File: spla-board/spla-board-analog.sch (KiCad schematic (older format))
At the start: 99 parts, among them J13 J_ANALOG, J14 J_AREF, J8 J_AREF_AMP, U51 ADC1173, U52 ADC1173, U53 ADC1173, U61 LMH6611, U62 LMH6611, U63 LMH6611, U74 LMH6611, U75 LMH6611, U76 TLV73333PDBV

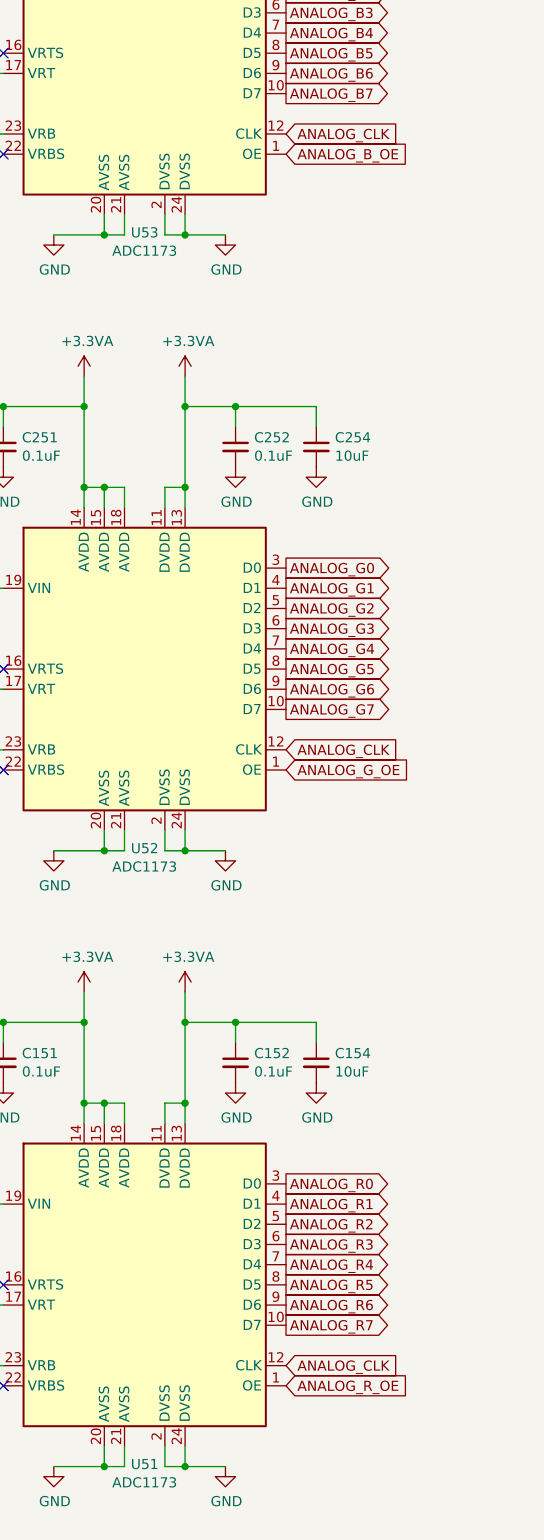
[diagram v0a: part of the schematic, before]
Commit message: schematic/pcb: Consolidate analog output-enable nets, and add a pullup resistor.
Note that this leaves two FPGA pins unused, which I'll need to correct later.
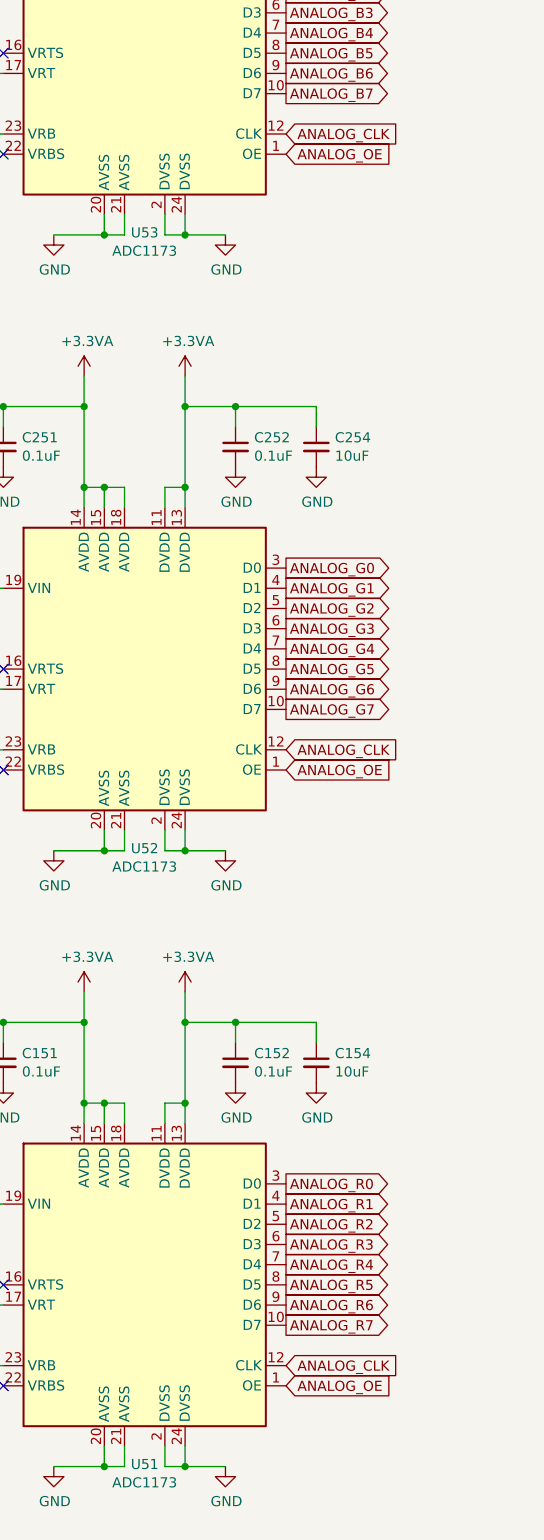
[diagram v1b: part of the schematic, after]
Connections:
- net ANALOG_G_OE is gone; now on net ANALOG_OE: U52.1 (OE)
- net ANALOG_R_OE is gone; now on net ANALOG_OE: U51.1 (OE)
- net ANALOG_B_OE renamed ANALOG_OE
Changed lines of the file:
@@
 RC low-pass filter\nCutoff = 1/(2*pi*R109*C109) = 18.55MHz\nWith Rxxx = 22 and Cxxx = 390pF\nNOSTUFF for now; left in as an option.
 Text GLabel 15000 3050 2    50   Input ~ 0
-ANALOG_B_OE
+ANALOG_OE
 Text GLabel 15000 6100 2    50   Input ~ 0
-ANALOG_G_OE
+ANALOG_OE
 Text GLabel 15000 9150 2    50   Input ~ 0
-ANALOG_R_OE
+ANALOG_OE
 Wire Wire Line
 	9450 7050 9450 7150

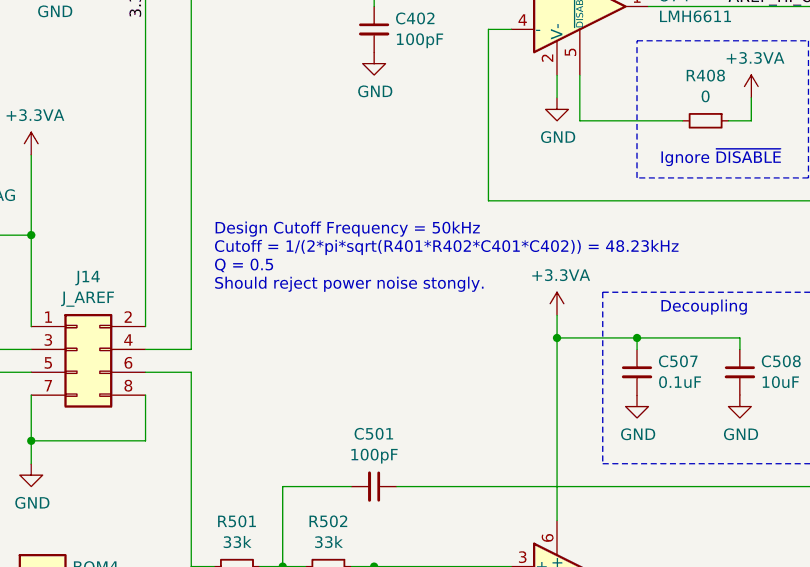
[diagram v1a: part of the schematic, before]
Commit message: schematic: Fix typo.
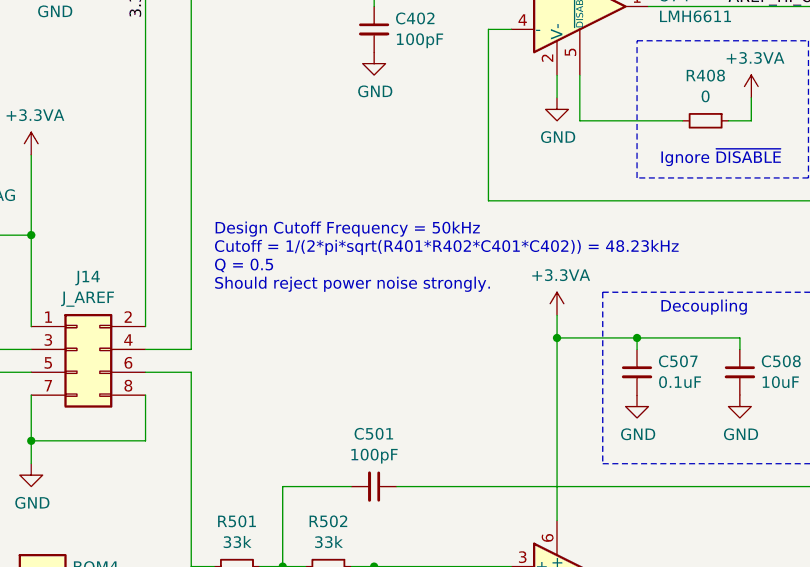
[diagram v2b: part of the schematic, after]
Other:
- note added: "Design Cutoff Frequency = 50kHz\nCutoff = 1/(2*pi*sqrt(R401*R402*C401*C402)) = 48.23kHz\nQ = 0.5\nShould reject power noise strongly."
- note removed: "Design Cutoff Frequency = 50kHz\nCutoff = 1/(2*pi*sqrt(R401*R402*C401*C402)) = 48.23kHz\nQ = 0.5\nShould reject power noise stongly."
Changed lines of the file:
@@
 Ignore ~DISABLE~
 Text Notes 2700 8600 0    50   ~ 0
-Design Cutoff Frequency = 50kHz\nCutoff = 1/(2*pi*sqrt(R401*R402*C401*C402)) = 48.23kHz\nQ = 0.5\nShould reject power noise stongly.
+Design Cutoff Frequency = 50kHz\nCutoff = 1/(2*pi*sqrt(R401*R402*C401*C402)) = 48.23kHz\nQ = 0.5\nShould reject power noise strongly.
 Wire Wire Line
 	4200 6150 4200 6250

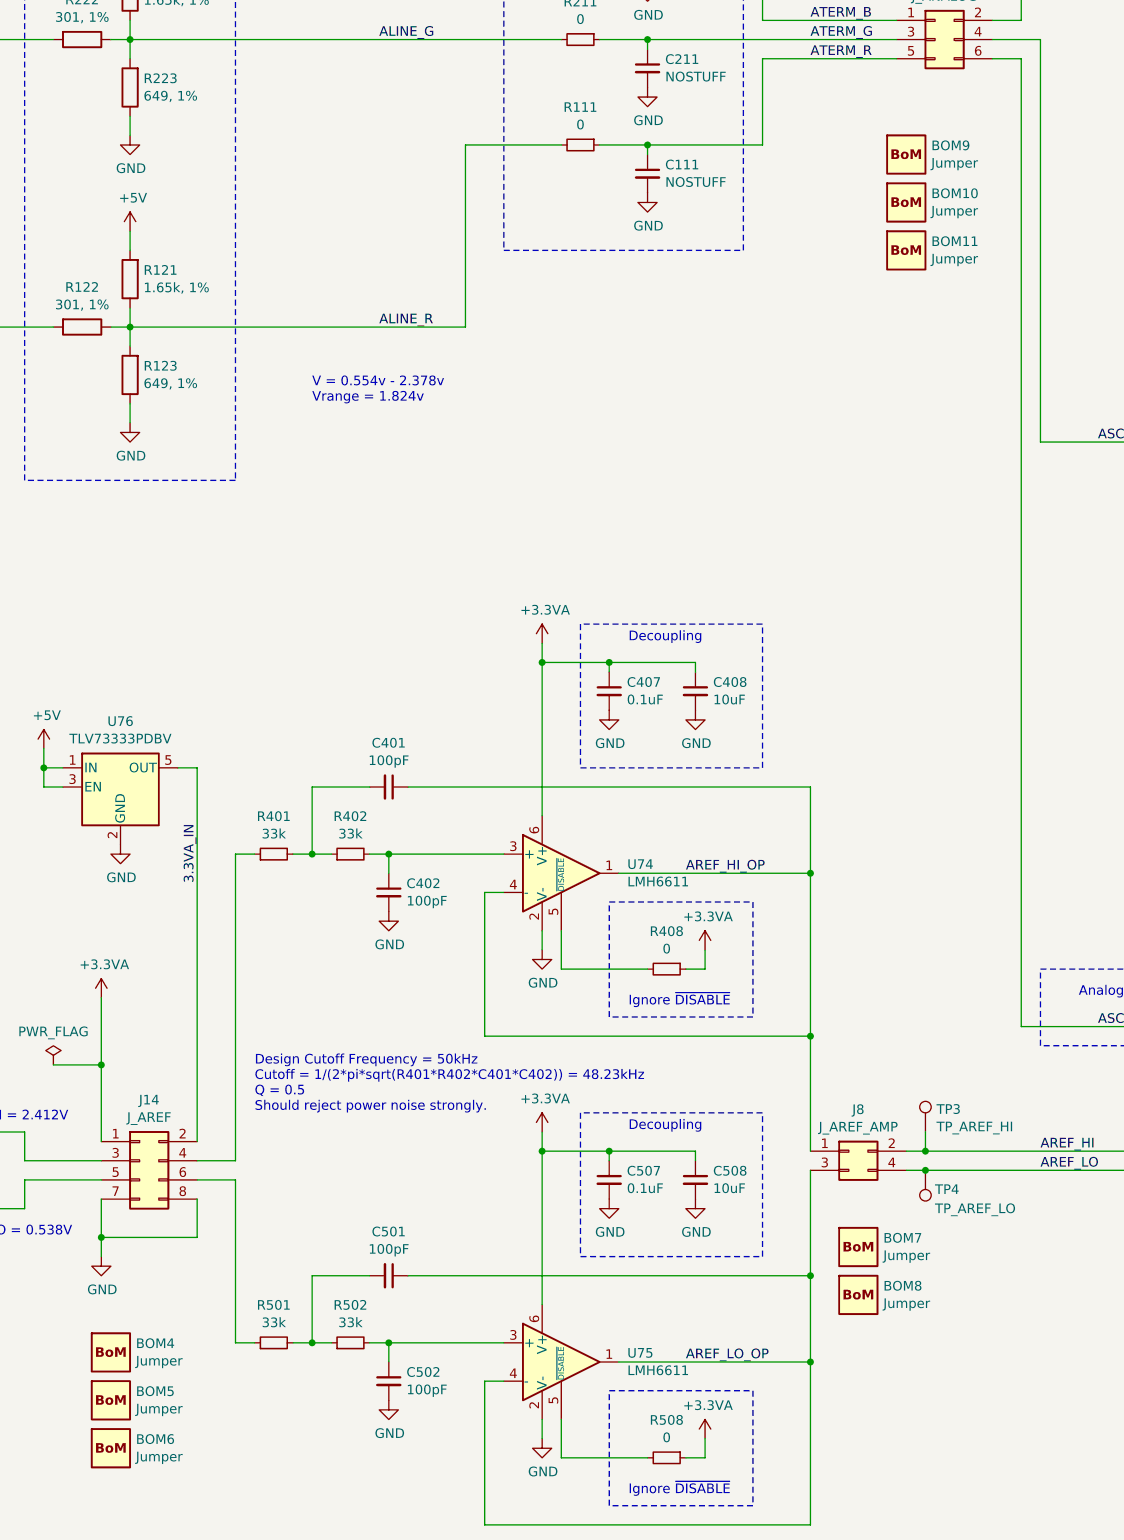
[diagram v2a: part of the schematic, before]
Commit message: schematic/pcb: Remove unnecessary 0-ohm resistors; renumber all parts by value.
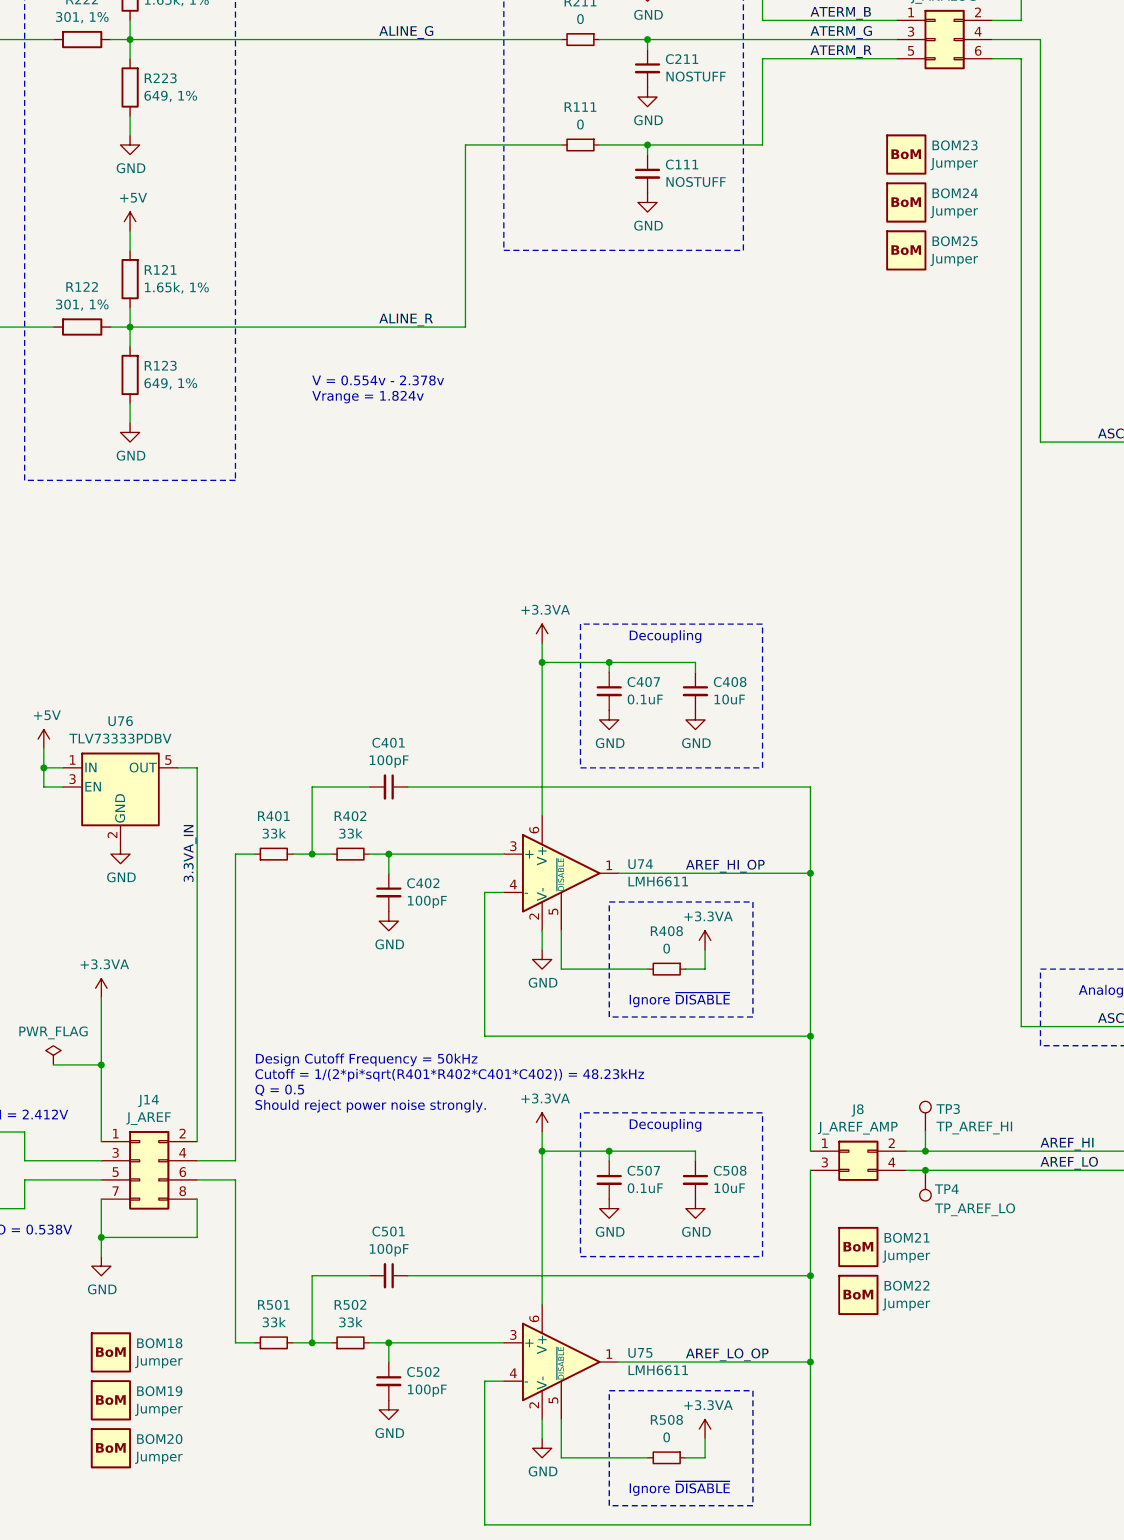
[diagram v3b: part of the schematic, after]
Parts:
- renumbered BOM4 to BOM18, BOM5 to BOM19, BOM6 to BOM20, BOM7 to BOM21, BOM8 to BOM22, BOM9 to BOM23, BOM10 to BOM24, BOM11 to BOM25
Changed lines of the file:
@@
 P 1950 9850
 AR Path="/5E50E589/5EB18261" Ref="BOM?"  Part="1"
-AR Path="/5E520B87/5EB18261" Ref="BOM4"  Part="1"
-F 0 "BOM4" H 2080 9896 50  0000 L CNN
+AR Path="/5E520B87/5EB18261" Ref="BOM18"  Part="1"
+F 0 "BOM18" H 2080 9896 50  0000 L CNN
 F 1 "Jumper" H 2080 9805 50  0000 L CNN
 F 2 "SPLA:BoM" H 1950 9850 50  0001 C CNN
@@
 P 1950 10100
 AR Path="/5E50E589/5EB36CC8" Ref="BOM?"  Part="1"
-AR Path="/5E520B87/5EB36CC8" Ref="BOM5"  Part="1"
-F 0 "BOM5" H 2080 10146 50  0000 L CNN
+AR Path="/5E520B87/5EB36CC8" Ref="BOM19"  Part="1"
+F 0 "BOM19" H 2080 10146 50  0000 L CNN
 F 1 "Jumper" H 2080 10055 50  0000 L CNN
 F 2 "SPLA:BoM" H 1950 10100 50  0001 C CNN
@@
 P 1950 10350
 AR Path="/5E50E589/5EB558F5" Ref="BOM?"  Part="1"
-AR Path="/5E520B87/5EB558F5" Ref="BOM6"  Part="1"
-F 0 "BOM6" H 2080 10396 50  0000 L CNN
+AR Path="/5E520B87/5EB558F5" Ref="BOM20"  Part="1"
+F 0 "BOM20" H 2080 10396 50  0000 L CNN
 F 1 "Jumper" H 2080 10305 50  0000 L CNN
 F 2 "SPLA:BoM" H 1950 10350 50  0001 C CNN
@@
 P 5850 9300
 AR Path="/5E50E589/5EB744FF" Ref="BOM?"  Part="1"
-AR Path="/5E520B87/5EB744FF" Ref="BOM7"  Part="1"
-F 0 "BOM7" H 5980 9346 50  0000 L CNN
+AR Path="/5E520B87/5EB744FF" Ref="BOM21"  Part="1"
+F 0 "BOM21" H 5980 9346 50  0000 L CNN
 F 1 "Jumper" H 5980 9255 50  0000 L CNN
 F 2 "SPLA:BoM" H 5850 9300 50  0001 C CNN
@@
 P 5850 9550
 AR Path="/5E50E589/5EB7450B" Ref="BOM?"  Part="1"
-AR Path="/5E520B87/5EB7450B" Ref="BOM8"  Part="1"
-F 0 "BOM8" H 5980 9596 50  0000 L CNN
+AR Path="/5E520B87/5EB7450B" Ref="BOM22"  Part="1"
+F 0 "BOM22" H 5980 9596 50  0000 L CNN
 F 1 "Jumper" H 5980 9505 50  0000 L CNN
 F 2 "SPLA:BoM" H 5850 9550 50  0001 C CNN
@@
 P 6100 3600
 AR Path="/5E50E589/5EB936B5" Ref="BOM?"  Part="1"
-AR Path="/5E520B87/5EB936B5" Ref="BOM9"  Part="1"
-F 0 "BOM9" H 6230 3646 50  0000 L CNN
+AR Path="/5E520B87/5EB936B5" Ref="BOM23"  Part="1"
+F 0 "BOM23" H 6230 3646 50  0000 L CNN
 F 1 "Jumper" H 6230 3555 50  0000 L CNN
 F 2 "SPLA:BoM" H 6100 3600 50  0001 C CNN
@@
 P 6100 3850
 AR Path="/5E50E589/5EBB26B8" Ref="BOM?"  Part="1"
-AR Path="/5E520B87/5EBB26B8" Ref="BOM10"  Part="1"
-F 0 "BOM10" H 6230 3896 50  0000 L CNN
+AR Path="/5E520B87/5EBB26B8" Ref="BOM24"  Part="1"
+F 0 "BOM24" H 6230 3896 50  0000 L CNN
 F 1 "Jumper" H 6230 3805 50  0000 L CNN
 F 2 "SPLA:BoM" H 6100 3850 50  0001 C CNN
@@
 P 6100 4100
 AR Path="/5E50E589/5EBD1242" Ref="BOM?"  Part="1"
-AR Path="/5E520B87/5EBD1242" Ref="BOM11"  Part="1"
-F 0 "BOM11" H 6230 4146 50  0000 L CNN
+AR Path="/5E520B87/5EBD1242" Ref="BOM25"  Part="1"
+F 0 "BOM25" H 6230 4146 50  0000 L CNN
 F 1 "Jumper" H 6230 4055 50  0000 L CNN
 F 2 "SPLA:BoM" H 6100 4100 50  0001 C CNN

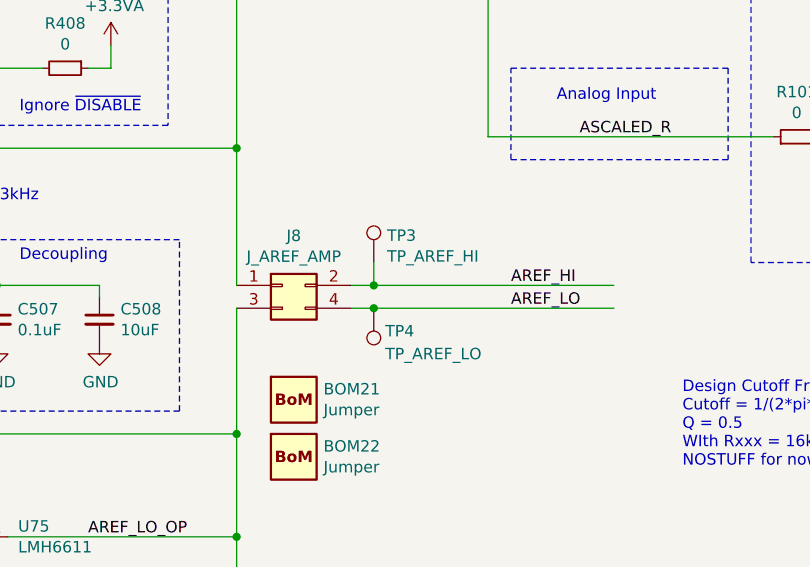
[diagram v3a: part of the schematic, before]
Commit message: schematic/pcb: Add 12mhz clock test point; renumber test points.
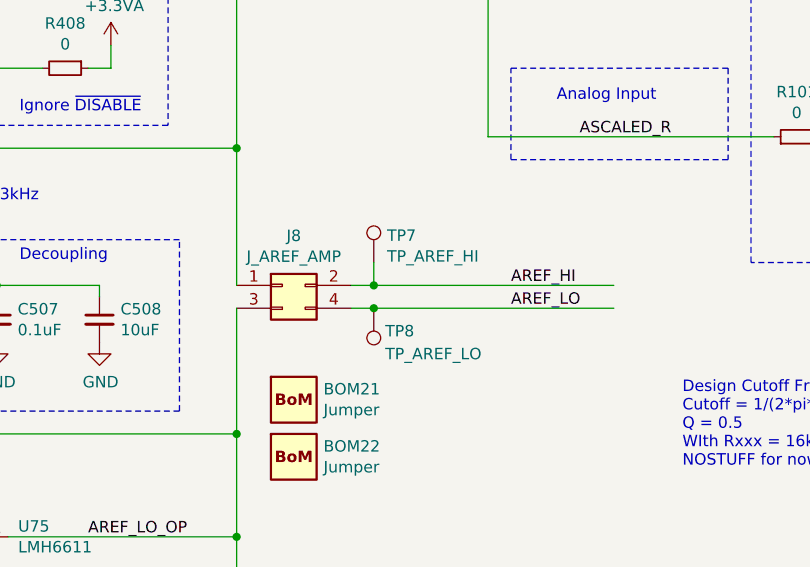
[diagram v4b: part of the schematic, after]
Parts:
- renumbered TP3 to TP7, TP4 to TP8
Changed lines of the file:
@@
 $EndComp
 $Comp
-L Connector:TestPoint TP3
+L Connector:TestPoint TP7
 U 1 1 5E6C3881
 P 6200 8700
-F 0 "TP3" H 6258 8818 50  0000 L CNN
+F 0 "TP7" H 6258 8818 50  0000 L CNN
 F 1 "TP_AREF_HI" H 6258 8727 50  0000 L CNN
 F 2 "TestPoint:TestPoint_Pad_D1.0mm" H 6400 8700 50  0001 C CNN
@@
 	2400 8850 2600 8850
 $Comp
-L Connector:TestPoint TP4
+L Connector:TestPoint TP8
 U 1 1 5E6D90A7
 P 6200 8900
-F 0 "TP4" H 6150 9000 50  0000 R CNN
+F 0 "TP8" H 6150 9000 50  0000 R CNN
 F 1 "TP_AREF_LO" H 6150 9100 50  0000 R CNN
 F 2 "TestPoint:TestPoint_Pad_D1.0mm" H 6400 8900 50  0001 C CNN
